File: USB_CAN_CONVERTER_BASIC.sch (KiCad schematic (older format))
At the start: 23 parts, among them P1 CONN_01X05, P2 CONN_01X02, P3 USB_A, P4 CONN_01X04, U1 STM32F042C6Ux, U2 PSD2CAN, U3 SN65HVD232D, U4 MCP1700T-3302E/TT, U5 USBLC6-2

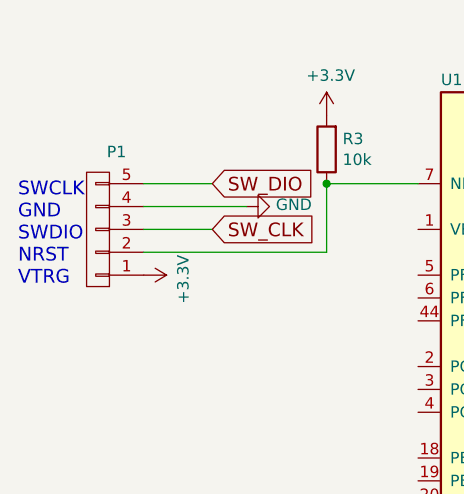
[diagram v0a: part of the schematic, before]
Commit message: Panel pcb addition and stencils.
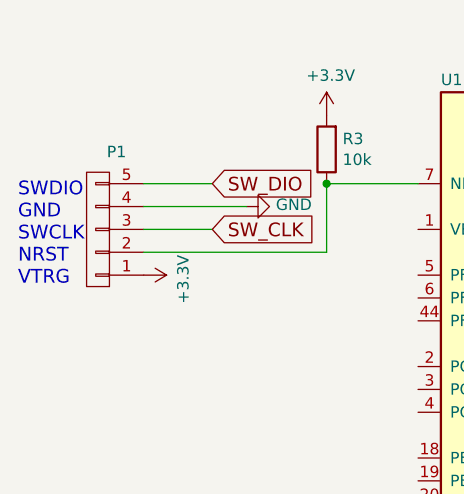
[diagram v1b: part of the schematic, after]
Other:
- note added: "SWDIO\nGND\nSWCLK\nNRST\nVTRG"
- note removed: "SWCLK\nGND\nSWDIO\nNRST\nVTRG"
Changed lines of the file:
@@
 $EndComp
 Text Notes 600  2300 0    60   ~ 0
-SWCLK\nGND\nSWDIO\nNRST\nVTRG
+SWDIO\nGND\nSWCLK\nNRST\nVTRG
 $Comp
 L GND #PWR02

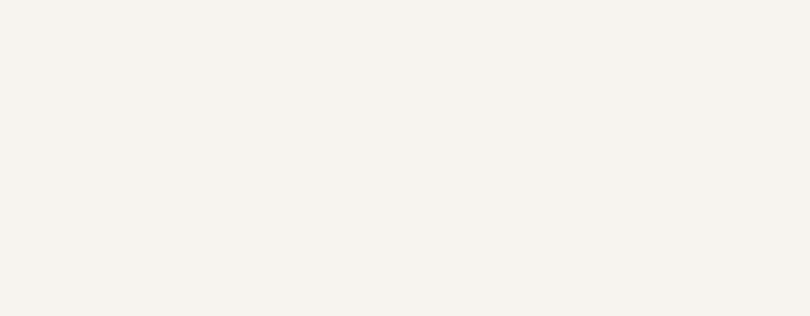
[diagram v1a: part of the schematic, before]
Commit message: Schematic name update
Schematic name update
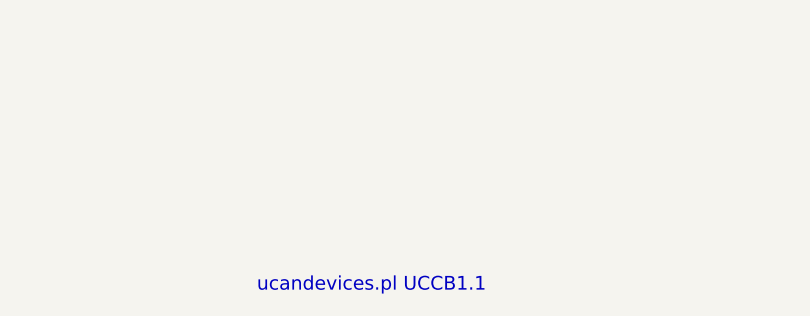
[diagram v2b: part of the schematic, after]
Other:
- note added: "ucandevices.pl UCCB1.1"
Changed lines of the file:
@@
 	1600 6350 1600 6200
 Connection ~ 1600 6200
+Text Notes 7400 7500 0    60   ~ 0
+ucandevices.pl UCCB1.1
 $EndSCHEMATC

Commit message: Fiducial Add
Fiducial Add
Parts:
- added F1: fiducial, Fiducials:Fiducial_1mm_Dia_2.54mm_Outer_CopperTop, symbol fiducial
- added F2: fiducial, Fiducials:Fiducial_1mm_Dia_2.54mm_Outer_CopperBottom, symbol fiducial
- U1: symbol STM32F042C6Ux -> STM32F042C6Ux-RESCUE-USB_CAN_CONVERTER_BASIC
- U3: value SN65HVD232D -> TCAN332
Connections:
- net CAN_MOD2: now reaches U1.30 (I2C1_SCL/TIM1_CH2/TSC_G4_IO1/USART1_TX/PA9)
- net CAN_MOD2: now also U3.5 (Vref)
- net at C1.2, R4.2, R5.1: no longer U3.5 (Vref)
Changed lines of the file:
@@
 EESchema Schematic File Version 2
+LIBS:USB_CAN_CONVERTER_BASIC-rescue
 LIBS:power
 LIBS:device
@@
 $EndDescr
 $Comp
-L STM32F042C6Ux U1
+L STM32F042C6Ux-RESCUE-USB_CAN_CONVERTER_BASIC U1
 U 1 1 570419FA
 P 5450 3150
@@
 P 3150 6150
 F 0 "U3" H 3150 6587 60  0000 C CNN
-F 1 "SN65HVD232D" H 3150 6481 60  0000 C CNN
+F 1 "TCAN332" H 3150 6481 60  0000 C CNN
 F 2 "SO:SO" H 3150 6481 60  0001 C CNN
 F 3 "" H 3000 6050 60  0000 C CNN
@@
 	0    -1   -1   0
 $EndComp
-$Comp
-L R R5
-U 1 1 5708DE1C
-P 2350 5650
-F 0 "R5" V 2450 5700 50  0000 R CNN
-F 1 "60R" V 2250 5700 50  0000 R CNN
-F 2 "Resistors_SMD:R_0805" H 2280 5741 50  0001 R CNN
-F 3 "" H 2350 5650 50  0000 C CNN
-	1    2350 5650
-	0    -1   -1   0
-$EndComp
-$Comp
-L C C1
-U 1 1 5708E07A
-P 2850 5550
-F 0 "C1" V 2750 5400 50  0000 L CNN
-F 1 "10n" V 3000 5450 50  0000 L CNN
-F 2 "Resistors_SMD:R_0805" H 2888 5400 50  0001 C CNN
-F 3 "" H 2850 5550 50  0000 C CNN
-	1    2850 5550
-	0    1    1    0
-$EndComp
-$Comp
-L GND #PWR019
-U 1 1 5708E325
-P 3000 5550
-F 0 "#PWR019" H 3000 5300 50  0001 C CNN
-F 1 "GND" V 3008 5422 50  0000 R CNN
-F 2 "" H 3000 5550 50  0000 C CNN
-F 3 "" H 3000 5550 50  0000 C CNN
-	1    3000 5550
-	1    0    0    -1
-$EndComp
 Text Notes 1650 5350 0    60   ~ 0
 CAN Terminator (optional)
@@
 $EndComp
 $Comp
-L +5V #PWR020
+L +5V #PWR019
 U 1 1 5716787A
 P 9200 4250
-F 0 "#PWR020" H 9200 4100 50  0001 C CNN
+F 0 "#PWR019" H 9200 4100 50  0001 C CNN
 F 1 "+5V" H 9100 4350 50  0000 C CNN
 F 2 "" H 9200 4250 50  0000 C CNN
@@
 $EndComp
 $Comp
-L GND #PWR021
+L GND #PWR020
 U 1 1 57167911
 P 10300 4250
-F 0 "#PWR021" H 10300 4000 50  0001 C CNN
+F 0 "#PWR020" H 10300 4000 50  0001 C CNN
 F 1 "GND" H 10250 4300 50  0000 C CNN
 F 2 "" H 10300 4250 50  0000 C CNN
@@
 $EndComp
 $Comp
-L GND #PWR022
+L GND #PWR021
 U 1 1 571ACD79
 P 9250 3350
-F 0 "#PWR022" H 9250 3100 50  0001 C CNN
+F 0 "#PWR021" H 9250 3100 50  0001 C CNN
 F 1 "GND" H 9350 3200 50  0000 C CNN
 F 2 "" H 9250 3350 50  0000 C CNN
@@
 $EndComp
 $Comp
-L +5V #PWR023
+L +5V #PWR022
 U 1 1 571E7816
 P 9400 3350
-F 0 "#PWR023" H 9400 3200 50  0001 C CNN
+F 0 "#PWR022" H 9400 3200 50  0001 C CNN
 F 1 "+5V" H 9418 3523 50  0000 C CNN
 F 2 "" H 9400 3350 50  0000 C CNN
@@
 $EndComp
 $Comp
-L +3.3V #PWR024
+L +3.3V #PWR023
 U 1 1 57800AA2
 P 1150 2250
-F 0 "#PWR024" H 1150 2100 50  0001 C CNN
+F 0 "#PWR023" H 1150 2100 50  0001 C CNN
 F 1 "+3.3V" H 1168 2423 50  0000 C CNN
 F 2 "" H 1150 2250 50  0000 C CNN
@@
 	1    1150 2250
 	0    1    1    0
-$EndComp
-$Comp
-L GS2 GS1
-U 1 1 5781392F
-P 1750 5850
-F 0 "GS1" H 1818 5850 50  0000 L CNN
-F 1 "GS2" H 1818 5850 50  0001 L CNN
-F 2 "Connect:GS2" H 1818 5805 50  0001 L CNN
-F 3 "" H 1750 5850 50  0000 C CNN
-	1    1750 5850
-	1    0    0    -1
-$EndComp
-$Comp
-L GS2 GS2
-U 1 1 57813F91
-P 2500 5850
-F 0 "GS2" H 2568 5850 50  0000 L CNN
-F 1 "GS2" H 2568 5850 50  0001 L CNN
-F 2 "Connect:GS2" H 2568 5805 50  0001 L CNN
-F 3 "" H 2500 5850 50  0000 C CNN
-	1    2500 5850
-	1    0    0    -1
 $EndComp
 $Comp
@@
 $EndComp
 $Comp
-L +3.3V #PWR025
+L +3.3V #PWR024
 U 1 1 578399EB
 P 10200 1950
-F 0 "#PWR025" H 10200 1800 50  0001 C CNN
+F 0 "#PWR024" H 10200 1800 50  0001 C CNN
 F 1 "+3.3V" H 10218 2123 50  0000 C CNN
 F 2 "" H 10200 1950 50  0000 C CNN
 F 3 "" H 10200 1950 50  0000 C CNN
 	1    10200 1950
+	1    0    0    -1
+$EndComp
+$Comp
+L +5V #PWR025
+U 1 1 5783A2C6
+P 10600 1950
+F 0 "#PWR025" H 10600 1800 50  0001 C CNN
+F 1 "+5V" H 10618 2123 50  0000 C CNN
+F 2 "" H 10600 1950 50  0000 C CNN
+F 3 "" H 10600 1950 50  0000 C CNN
+	1    10600 1950
+	1    0    0    -1
+$EndComp
+Text Notes 7400 7500 0    60   ~ 0
+ucandevices.pl UCCB1.1
+$Comp
+L fiducial F1
+U 1 1 58469840
+P 9950 750
+F 0 "F1" H 9750 1000 60  0001 C CNN
+F 1 "fiducial" H 10200 500 60  0001 C CNN
+F 2 "Fiducials:Fiducial_1mm_Dia_2.54mm_Outer_CopperTop" H 9950 750 60  0001 C CNN
+F 3 "" H 9950 750 60  0001 C CNN
+	1    9950 750
+	1    0    0    -1
+$EndComp
+$Comp
+L fiducial F2
+U 1 1 584699B5
+P 9600 750
+F 0 "F2" H 9400 1000 60  0001 C CNN
+F 1 "fiducial" H 9850 500 60  0001 C CNN
+F 2 "Fiducials:Fiducial_1mm_Dia_2.54mm_Outer_CopperBottom" H 9600 750 60  0001 C CNN
+F 3 "" H 9600 750 60  0001 C CNN
+	1    9600 750
+	1    0    0    -1
+$EndComp
+$Comp
+L GS2 GS2
+U 1 1 57813F91
+P 2500 5850
+F 0 "GS2" H 2568 5850 50  0000 L CNN
+F 1 "GS2" H 2568 5850 50  0001 L CNN
+F 2 "Connect:GS2" H 2568 5805 50  0001 L CNN
+F 3 "" H 2500 5850 50  0000 C CNN
+	1    2500 5850
+	1    0    0    -1
+$EndComp
+$Comp
+L GS2 GS1
+U 1 1 5781392F
+P 1750 5850
+F 0 "GS1" H 1818 5850 50  0000 L CNN
+F 1 "GS2" H 1818 5850 50  0001 L CNN
+F 2 "Connect:GS2" H 1818 5805 50  0001 L CNN
+F 3 "" H 1750 5850 50  0000 C CNN
+	1    1750 5850
 	1    0    0    -1
 $EndComp
@@
 Connection ~ 2500 6100
 Connection ~ 1750 6200
-Wire Wire Line
-	2150 5550 2700 5550
-Wire Wire Line
-	2700 5550 2700 6000
-Connection ~ 2150 5650
 Wire Notes Line
 	1600 5450 1600 5850
@@
 Wire Wire Line
 	1450 1850 1150 1850
-Connection ~ 2700 5550
-Wire Wire Line
-	2150 5550 2150 5650
 Wire Wire Line
 	2050 5650 2200 5650
@@
 Wire Wire Line
 	2500 6050 2500 6100
-$Comp
-L +5V #PWR026
-U 1 1 5783A2C6
-P 10600 1950
-F 0 "#PWR026" H 10600 1800 50  0001 C CNN
-F 1 "+5V" H 10618 2123 50  0000 C CNN
-F 2 "" H 10600 1950 50  0000 C CNN
-F 3 "" H 10600 1950 50  0000 C CNN
-	1    10600 1950
-	1    0    0    -1
-$EndComp
 Wire Wire Line
 	8750 3550 8750 3250
@@
 	1600 6350 1600 6200
 Connection ~ 1600 6200
-Text Notes 7400 7500 0    60   ~ 0
-ucandevices.pl UCCB1.1
+Wire Wire Line
+	2150 5550 2150 5650
+Connection ~ 2150 5650
+$Comp
+L R R5
+U 1 1 5708DE1C
+P 2350 5650
+F 0 "R5" V 2450 5700 50  0000 R CNN
+F 1 "60R" V 2250 5700 50  0000 R CNN
+F 2 "Resistors_SMD:R_0805" H 2280 5741 50  0001 R CNN
+F 3 "" H 2350 5650 50  0000 C CNN
+	1    2350 5650
+	0    -1   -1   0
+$EndComp
+$Comp
+L GND #PWR026
+U 1 1 5708E325
+P 3000 5550
+F 0 "#PWR026" H 3000 5300 50  0001 C CNN
+F 1 "GND" V 3008 5422 50  0000 R CNN
+F 2 "" H 3000 5550 50  0000 C CNN
+F 3 "" H 3000 5550 50  0000 C CNN
+	1    3000 5550
+	1    0    0    -1
+$EndComp
+$Comp
+L C C1
+U 1 1 5708E07A
+P 2850 5550
+F 0 "C1" V 2750 5400 50  0000 L CNN
+F 1 "10n" V 3000 5450 50  0000 L CNN
+F 2 "Resistors_SMD:R_0805" H 2888 5400 50  0001 C CNN
+F 3 "" H 2850 5550 50  0000 C CNN
+	1    2850 5550
+	0    1    1    0
+$EndComp
+Wire Wire Line
+	2150 5550 2700 5550
+Text GLabel 2700 6000 0    60   Input ~ 0
+CAN_MOD2
+Text GLabel 8550 3950 2    60   Input ~ 0
+CAN_MOD2
 $EndSCHEMATC

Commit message: components description update
components description update
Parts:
- removed C1: 10n, Resistors_SMD:R_0805, symbol C
- removed GS2: GS2, Connect:GS2, symbol GS2
- removed R5: 60R, Resistors_SMD:R_0805, symbol R
- C2, C5: 1st Disrtib Link (none) -> http://www.tme.eu/en/details/c0805c104k3rac/0805-mlcc-smd-c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; 1st Disrtib PN (none) -> TME; Description (none) -> 100nF 25V 805; MFG (none) -> KEMET; MFG Part Num (none) -> C0805C104K3RAC
- C3: value 10u -> 10n; 1st Disrtib Link (none) -> http://www.tme.eu/en/details/08053c103kat2a/0805-mlcc-smd-c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; 1st Disrtib PN (none) -> TME; Description (none) -> 10nF 25V 805; MFG (none) -> AVX; MFG Part Num (none) -> 08053C103KAT2A
- C4: 1st Disrtib Link (none) -> http://www.tme.eu/en/details/08053c103kat2a/0805-mlcc-smd-c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; 1st Disrtib PN (none) -> TME; Description (none) -> 10nF 25V 805; MFG (none) -> AVX; MFG Part Num (none) -> 08053C103KAT2A
- C7, C8: 1st Disrtib Link (none) -> http://www.tme.eu/en/details/08053g105zat2a/0805-mlcc-smd-c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; 1st Disrtib PN (none) -> TME; Description (none) -> 1uF 25V 805; MFG (none) -> AVX; MFG Part Num (none) -> 08053G105ZAT2A
- L1: 1st Disrtib Link (none) -> http://www.tme.eu/en/details/dl0805-0.82/smd-0805-inductors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; 1st Disrtib PN (none) -> TME; Description (none) -> 0.82uH 150mA 0805; MFG (none) -> FERROCORE; MFG Part Num (none) -> DL0805-0.82
- P2: 1st Disrtib Link (none) -> http://www.tme.eu/en/details/dg126-5.0-2p14/terminal-blocks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; 1st Disrtib PN (none) -> TME; Description (none) -> Terminal block; 5mm; angled; 0.5÷2.5mm2; ways:2; H:10.9mm; 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; MFG (none) -> DEGSON ELECTRONICS; MFG Part Num (none) -> DG126-5.0-2P14
- P3: 1st Disrtib Link (none) -> http://www.tme.eu/en/details/usba-lp/usb-ieee1394-connector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; 1st Disrtib PN (none) -> TME; Description (none) -> Plug; USB A; THT; angled 90°; 1.5A; Contacts: phosphor bron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; MFG (none) -> CONNFLY; MFG Part Num (none) -> DS1097-BN0
- R3: 1st Disrtib Link (none) -> http://www.tme.eu/en/details/crcw080510k0fkea/0805-smd-resi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; 1st Disrtib PN (none) -> TME; Description (none) -> 10K 0.125W 805; MFG (none) -> VISHAY; MFG Part Num (none) -> CRCW080510K0FKEA
- R4: value 60R -> 120R; 1st Disrtib Link (none) -> http://www.tme.eu/en/details/smd0805-120r/0805-smd-resistor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; 1st Disrtib PN (none) -> TME; Description (none) -> 120R 0.125W 805; MFG (none) -> ROYAL OHM; MFG Part Num (none) -> SMD0805-120R
- U1: 1st Disrtib Link (none) -> http://www.tme.eu/pl/details/stm32f042c6u6/mikrokontrolery-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; 1st Disrtib PN (none) -> TME; MFG (none) -> ST; MFG Part Num (none) -> STM32F042C6U6
- U2: value PSD2CAN -> PESD2CAN; 1st Disrtib Link (none) -> http://www.tme.eu/en/details/pesd2can/bidirectional-smd-tra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; 1st Disrtib PN (none) -> TME; MFG (none) -> NXP; MFG Part Num (none) -> PESD2CAN.215
- U3: 1st Disrtib Link (none) -> http://pl.farnell.com/texas-instruments/tcan332dr/can-trans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; 1st Disrtib PN (none) -> Farnell; MFG (none) -> TI; MFG Part Num (none) -> TCAN332DR
- U4: 1st Disrtib Link (none) -> http://pl.farnell.com/microchip/mcp1700t-3302e-tt/ic-v-reg-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; 1st Disrtib PN (none) -> Farnell; MFG (none) -> MICROCHIP; MFG Part Num (none) -> MCP1700T-3302E/TT
- U5: value USBLC6-2 -> USBLC6-2SC6; 1st Disrtib Link (none) -> http://www.tme.eu/en/details/usblc6-2sc6/supervisor-circuit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; 1st Disrtib PN (none) -> TME; MFG (none) -> ST; MFG Part Num (none) -> USBLC6-2SC6
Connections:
- net at P2.1 (P1), U2.1 (C1), U3.6 (CANL): now also R4.2

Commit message: Update Outputs
Update Outputs
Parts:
- C2: Description 100nF 25V 805 -> 100nF 25V 805 10%
- C3: Description 10nF 25V 805 -> 10nF 25V 805 10%
- C4: value 10nC -> 10n; Description 10nF 25V 805 -> 10nF 25V 805 10%
- C5: value 100nC -> 100n; footprint Resistors_SMD:R_0805_HandSoldering -> Resistors_SMD:R_0805; Description 100nF 25V 805 -> 100nF 25V 805 10%
- C7, C8: value 1uC -> 1u
- P2: Description Terminal block; 5mm; angled; 0.5÷2.5mm2; ways:2; H:10.9mm; 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 -> Terminal block 5mm angled 0.5÷2.5mm2 ways:2 H:10.9mm green
- P3: Description Plug; USB A; THT; angled 90°; 1.5A; Contacts: phosphor bron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 -> Plug USB A THT angled 90° 1.5A Contacts: phosphor bronze 500
- R3: Description 10K 0.125W 805 -> 10K 0.125W 805 10%
- R4: Description 120R 0.125W 805 -> 120R 0.125W 805 5%
- U1: footprint Housings_DFN_QFN:QFN-48-1EP_7x7mm_Pitch0.5mm -> usb_ccb_custom:QFN-48-1EP_7x7mm_Pitch0.5mm
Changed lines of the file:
@@
 F 0 "U1" H 2450 4875 50  0000 L BNN
 F 1 "STM32F042C6Ux" H 8450 4875 50  0000 R BNN
-F 2 "Housings_DFN_QFN:QFN-48-1EP_7x7mm_Pitch0.5mm" H 8450 4825 50  0000 R TNN
+F 2 "usb_ccb_custom:QFN-48-1EP_7x7mm_Pitch0.5mm" H 8450 4825 50  0000 R TNN
 F 3 "" H 5450 3150 50  0000 C CNN
 F 4 "STM32F042C6U6" H 5450 3150 60  0001 C CNN "MFG Part Num"
@@
 F 6 "http://www.tme.eu/en/details/crcw080510k0fkea/0805-smd-resistors/vishay/" H 1950 1700 60  0001 C CNN "1st Disrtib Link"
 F 7 "TME" H 1950 1700 60  0001 C CNN "1st Disrtib PN"
-F 8 "10K 0.125W 805" H 1950 1700 60  0001 C CNN "Description"
+F 8 "10K 0.125W 805 10%" H 1950 1700 60  0001 C CNN "Description"
 	1    1950 1700
 	-1   0    0    1
@@
 F 6 "http://www.tme.eu/en/details/usba-lp/usb-ieee1394-connectors/connfly/ds1097-bn0/" H 10800 4250 60  0001 C CNN "1st Disrtib Link"
 F 7 "TME" H 10800 4250 60  0001 C CNN "1st Disrtib PN"
-F 8 "Plug; USB A; THT; angled 90°; 1.5A; Contacts: phosphor bronze; 500" H 10800 4250 60  0001 C CNN "Description"
+F 8 "Plug USB A THT angled 90° 1.5A Contacts: phosphor bronze 500" H 10800 4250 60  0001 C CNN "Description"
 	1    10800 4250
 	0    1    1    0
@@
 F 6 "http://www.tme.eu/en/details/dg126-5.0-2p14/terminal-blocks-pcb-mount/degson-electronics/dg126-50-02p-14-00a/" H 950 6150 60  0001 C CNN "1st Disrtib Link"
 F 7 "TME" H 950 6150 60  0001 C CNN "1st Disrtib PN"
-F 8 "Terminal block; 5mm; angled; 0.5÷2.5mm2; ways:2; H:10.9mm; green" H 950 6150 60  0001 C CNN "Description"
+F 8 "Terminal block 5mm angled 0.5÷2.5mm2 ways:2 H:10.9mm green" H 950 6150 60  0001 C CNN "Description"
 	1    950  6150
 	-1   0    0    -1
@@
 P 9100 1700
 F 0 "C4" H 9215 1746 50  0000 L CNN
-F 1 "10nC" H 9215 1655 50  0000 L CNN
+F 1 "10n" H 9215 1655 50  0000 L CNN
 F 2 "Resistors_SMD:R_0805" H 9138 1550 50  0001 C CNN
 F 3 "" H 9100 1700 50  0000 C CNN
@@
 F 6 "http://www.tme.eu/en/details/08053c103kat2a/0805-mlcc-smd-capacitors/avx/" H 9100 1700 60  0001 C CNN "1st Disrtib Link"
 F 7 "TME" H 9100 1700 60  0001 C CNN "1st Disrtib PN"
-F 8 "10nF 25V 805" H 9100 1700 60  0001 C CNN "Description"
+F 8 "10nF 25V 805 10%" H 9100 1700 60  0001 C CNN "Description"
 	1    9100 1700
 	1    0    0    -1
@@
 P 9500 1700
 F 0 "C5" H 9615 1746 50  0000 L CNN
-F 1 "100nC" H 9615 1655 50  0000 L CNN
-F 2 "Resistors_SMD:R_0805_HandSoldering" H 9538 1550 50  0001 C CNN
+F 1 "100n" H 9615 1655 50  0000 L CNN
+F 2 "Resistors_SMD:R_0805" H 9538 1550 50  0001 C CNN
 F 3 "" H 9500 1700 50  0000 C CNN
 F 4 "C0805C104K3RAC" H 9500 1700 60  0001 C CNN "MFG Part Num"
@@
 F 6 "http://www.tme.eu/en/details/c0805c104k3rac/0805-mlcc-smd-capacitors/kemet/c0805c104k3ractu/" H 9500 1700 60  0001 C CNN "1st Disrtib Link"
 F 7 "TME" H 9500 1700 60  0001 C CNN "1st Disrtib PN"
-F 8 "100nF 25V 805" H 9500 1700 60  0001 C CNN "Description"
+F 8 "100nF 25V 805 10%" H 9500 1700 60  0001 C CNN "Description"
 	1    9500 1700
 	1    0    0    -1
@@
 P 10550 2800
 F 0 "C8" H 10665 2846 50  0000 L CNN
-F 1 "1uC" H 10665 2755 50  0000 L CNN
+F 1 "1u" H 10665 2755 50  0000 L CNN
 F 2 "Resistors_SMD:R_0805" H 10588 2650 50  0001 C CNN
 F 3 "" H 10550 2800 50  0000 C CNN
@@
 P 9750 2800
 F 0 "C7" H 9550 2850 50  0000 L CNN
-F 1 "1uC" H 9500 2750 50  0000 L CNN
+F 1 "1u" H 9500 2750 50  0000 L CNN
 F 2 "Resistors_SMD:R_0805" H 9788 2650 50  0001 C CNN
 F 3 "" H 9750 2800 50  0000 C CNN
@@
 F 6 "http://www.tme.eu/en/details/08053c103kat2a/0805-mlcc-smd-capacitors/avx/" H 4750 6250 60  0001 C CNN "1st Disrtib Link"
 F 7 "TME" H 4750 6250 60  0001 C CNN "1st Disrtib PN"
-F 8 "10nF 25V 805" H 4750 6250 60  0001 C CNN "Description"
+F 8 "10nF 25V 805 10%" H 4750 6250 60  0001 C CNN "Description"
 	1    4750 6250
 	1    0    0    -1
@@
 F 6 "http://www.tme.eu/en/details/c0805c104k3rac/0805-mlcc-smd-capacitors/kemet/c0805c104k3ractu/" H 4450 6250 60  0001 C CNN "1st Disrtib Link"
 F 7 "TME" H 4450 6250 60  0001 C CNN "1st Disrtib PN"
-F 8 "100nF 25V 805" H 4450 6250 60  0001 C CNN "Description"
+F 8 "100nF 25V 805 10%" H 4450 6250 60  0001 C CNN "Description"
 	1    4450 6250
 	1    0    0    -1
@@
 F 6 "http://www.tme.eu/en/details/smd0805-120r/0805-smd-resistors/royal-ohm/0805s8j0121t5e/" H 1900 5650 60  0001 C CNN "1st Disrtib Link"
 F 7 "TME" H 1900 5650 60  0001 C CNN "1st Disrtib PN"
-F 8 "120R 0.125W 805" H 1900 5650 60  0001 C CNN "Description"
+F 8 "120R 0.125W 805 5%" H 1900 5650 60  0001 C CNN "Description"
 	1    1900 5650
 	0    -1   -1   0
